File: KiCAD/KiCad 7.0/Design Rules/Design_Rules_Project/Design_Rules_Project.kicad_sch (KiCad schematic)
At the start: 2 parts, among them J1 2.54mm spaced headers, J2 1mm diameter

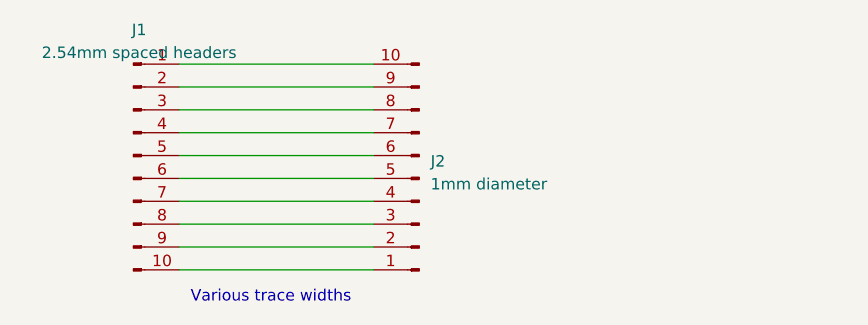
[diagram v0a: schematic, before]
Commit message: Fix clearance with fill zones
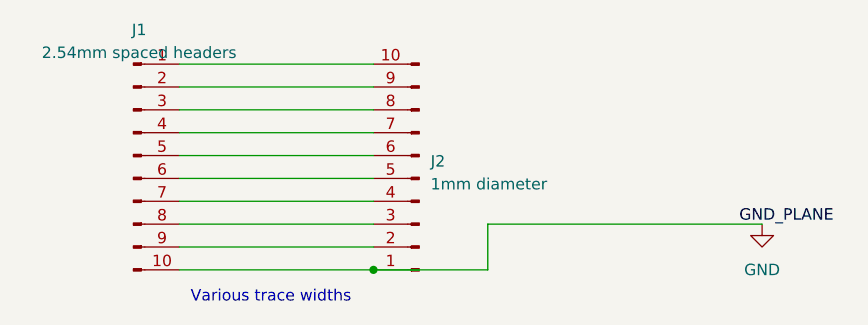
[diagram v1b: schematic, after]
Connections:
- net GND: now reaches J1.10 (Pin_10), J2.1 (Pin_1)
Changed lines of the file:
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@@
 (kicad_sch (version 20230121) (generator eeschema)
   (paper "A4")
+  (junction (at 87.63 87.63) (diameter 0) (color 0 0 0 0)
+  )
+  (wire (pts (xy 100.33 82.55) (xy 100.33 87.63))
+    (stroke (width 0) (type default))
+  )
   (wire (pts (xy 66.04 77.47) (xy 87.63 77.47))
     (stroke (width 0) (type default))
@@
     (stroke (width 0) (type default))
   )
+  (wire (pts (xy 100.33 82.55) (xy 130.81 82.55))
+    (stroke (width 0) (type default))
+  )
   (wire (pts (xy 66.04 82.55) (xy 87.63 82.55))
     (stroke (width 0) (type default))
@@
     (stroke (width 0) (type default))
   )
+  (wire (pts (xy 100.33 87.63) (xy 87.63 87.63))
+    (stroke (width 0) (type default))
+  )
   (wire (pts (xy 66.04 74.93) (xy 87.63 74.93))
     (stroke (width 0) (type default))
   )
   (text "Various trace widths" (at 67.31 91.44 0)
+    (effects (font (size 1.27 1.27)) (justify left bottom))
+  )
+  (label "GND_PLANE" (at 128.27 82.55 0) (fields_autoplaced)
     (effects (font (size 1.27 1.27)) (justify left bottom))
   )
@@
         )
       )
+    )
+  )
+  (symbol (lib_id "power:GND") (at 130.81 82.55 0) (unit 1)
+    (in_bom yes) (on_board yes) (dnp no) (fields_autoplaced)
+    (property "Reference" "#PWR01" (at 130.81 88.9 0)
+      (effects (font (size 1.27 1.27)) hide)
+    )
+    (property "Value" "GND" (at 130.81 87.63 0)
+      (effects (font (size 1.27 1.27)))
+    )
+    (property "Footprint" "" (at 130.81 82.55 0)
+      (effects (font (size 1.27 1.27)) hide)
+    )
+    (property "Datasheet" "" (at 130.81 82.55 0)
+      (effects (font (size 1.27 1.27)) hide)
+    )
+    (pin "1")
+    (instances
+      (project "Design_Rules_Project"
+        (path "/73e94abe-1b5c-4e4f-8683-3242f4640954"
+          (reference "#PWR01") (unit 1)
+        )
+      )
